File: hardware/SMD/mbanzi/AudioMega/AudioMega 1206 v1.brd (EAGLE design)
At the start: 60 x 58 mm, 72 parts, among them Q1 BC846ASMD, Q2 BC846ASMD, Q3 BC846ASMD, Q4 2N7002, Q5 BC846ASMD, Q6 BC846ASMD, U1 REG1117-5, U2 REG1117-3.3, U3 ATMEGA328-AU, U4 LM386M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

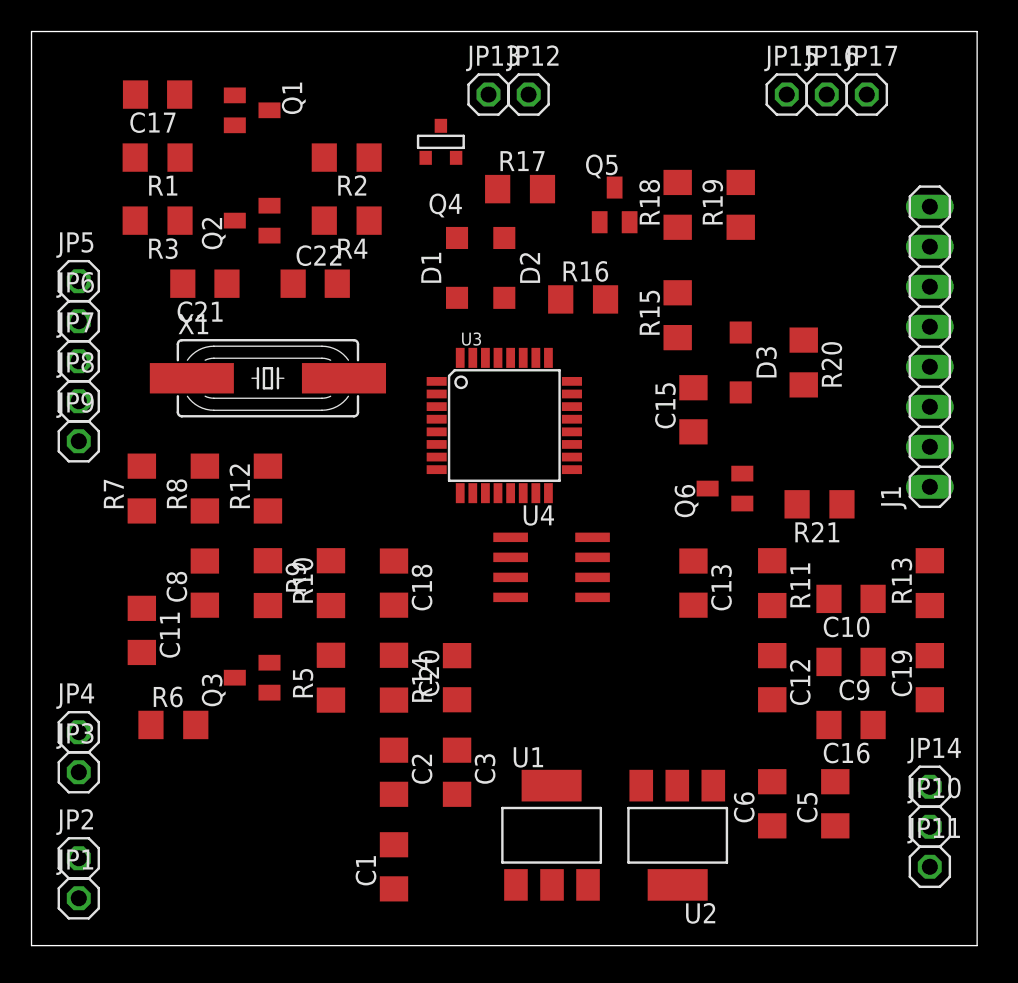
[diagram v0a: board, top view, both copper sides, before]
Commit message: Created initial 1206 version of the PCB & renamed files
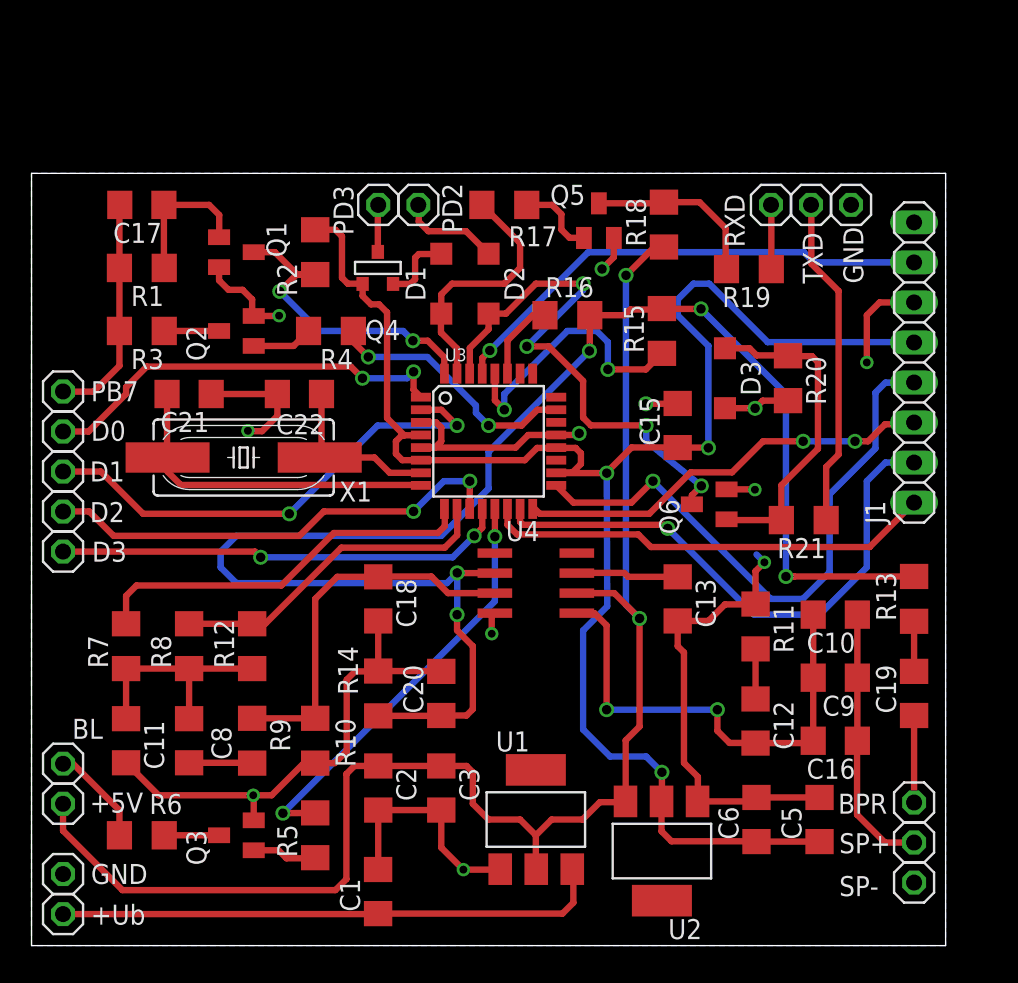
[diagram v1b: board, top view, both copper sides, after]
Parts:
- moved C8 10.0 mm to (10.0, 13.0)
- moved Q3 10.0 mm to (13.0, 7.00)
- moved R10 10.0 mm to (18.0, 13.0)
- moved R12 10.0 mm to (14.0, 19.0)
- moved R5 10.0 mm to (18.0, 7.00)
- moved R7 10.0 mm to (6.00, 19.0)
- moved R8 10.0 mm to (10.0, 19.0)
- moved R9 10.0 mm to (14.0, 13.0)
- moved JP12 9.90 mm to (24.5, 47.0)
- moved JP13 9.90 mm to (22.0, 47.0)
- moved Q1 9.06 mm to (13.0, 44.0)
- moved Q4 8.94 mm to (22.0, 43.0)
- moved R6 7.28 mm to (7.00, 7.00)
- moved C11 7.07 mm to (6.00, 13.0)
- moved C17 7.07 mm to (7.00, 47.0)
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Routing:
- net GND: track 0.00 -> 121.1 mm, vias 0 -> 12
- net +3V3: track 0.00 -> 109.0 mm, vias 0 -> 3
- net VOL_B: track 0.00 -> 101.2 mm, vias 0 -> 5
- net +5V: track 0.00 -> 94.1 mm, vias 0 -> 2
- net N$5: track 0.00 -> 37.5 mm, vias 0 -> 1
- net N$3: track 0.00 -> 35.5 mm, vias 0 -> 1
- net N$32: track 0.00 -> 34.8 mm
- net N$42: track 0.00 -> 34.7 mm, vias 0 -> 4
- net N$6: track 0.00 -> 31.4 mm, vias 0 -> 1
- net N$35: track 0.00 -> 31.1 mm, vias 0 -> 2
- net N$17: track 0.00 -> 30.4 mm, vias 0 -> 2
- net N$31: track 0.00 -> 29.7 mm, vias 0 -> 2
- net N$30: track 0.00 -> 28.7 mm, vias 0 -> 2
- net N$2: track 0.00 -> 28.6 mm
- net N$34: track 0.00 -> 26.9 mm, vias 0 -> 2
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- added copper zone on layer 16, net GND
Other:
- board size 60 x 58 mm -> 58 x 49 mm
- board text added: "+5V"
- board text added: "+Ub"
- board text added: "AudioMega v1.0"
- board text added: "BL"
- board text added: "BPR"
- board text added: "D0"
- board text added: "D1"
- board text added: "D2"
- board text added: "D3"
- board text added: "GND"
- board text added: "PB7"
- board text added: "PD2"
- board text added: "PD3"
- board text added: "RXD"
- board text added: "SP+"
- board text added: "SP-"
- board text added: "TXD"
